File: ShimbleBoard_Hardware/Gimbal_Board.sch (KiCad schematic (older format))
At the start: 85 parts, among them Q1 Q_NMOS_GDS, Q2 Q_NMOS_GDS, Q3 Q_NMOS_GDS, Q4 Q_NMOS_GDS, Q5 Q_NMOS_GDS, Q6 Q_NMOS_GDS, Q7 Q_NMOS_GDS, Q8 Q_NMOS_GDS, SW1 SW_Push, SW10 SW_SPDT, SW2 SW_Push, SW3 SW_Push, SW4 SW_Push, SW5 SW_Push, SW6 SW_Push, SW7 SW_Push, SW8 SW_Push, SW9 SW_Push, U1 TM4C129E_Launchpad, U2 OKI, U3 OKI

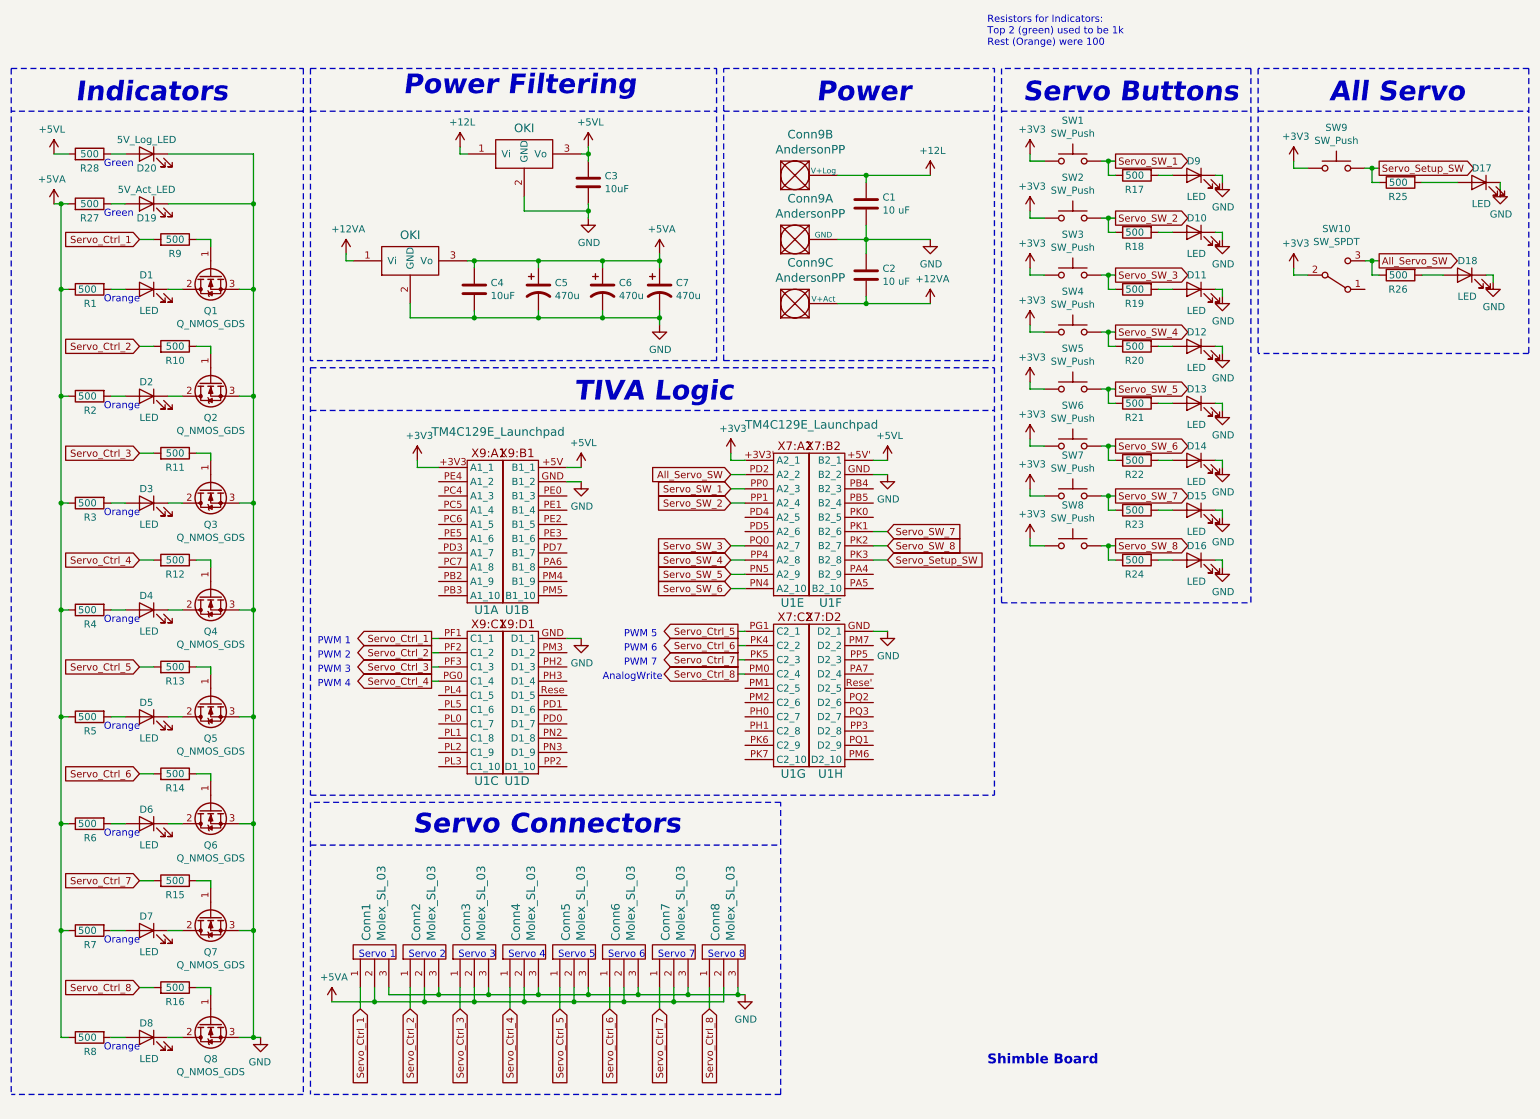
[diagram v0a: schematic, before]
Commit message: Changed the LED's to 5VL and fixed the wiring for it and added X's
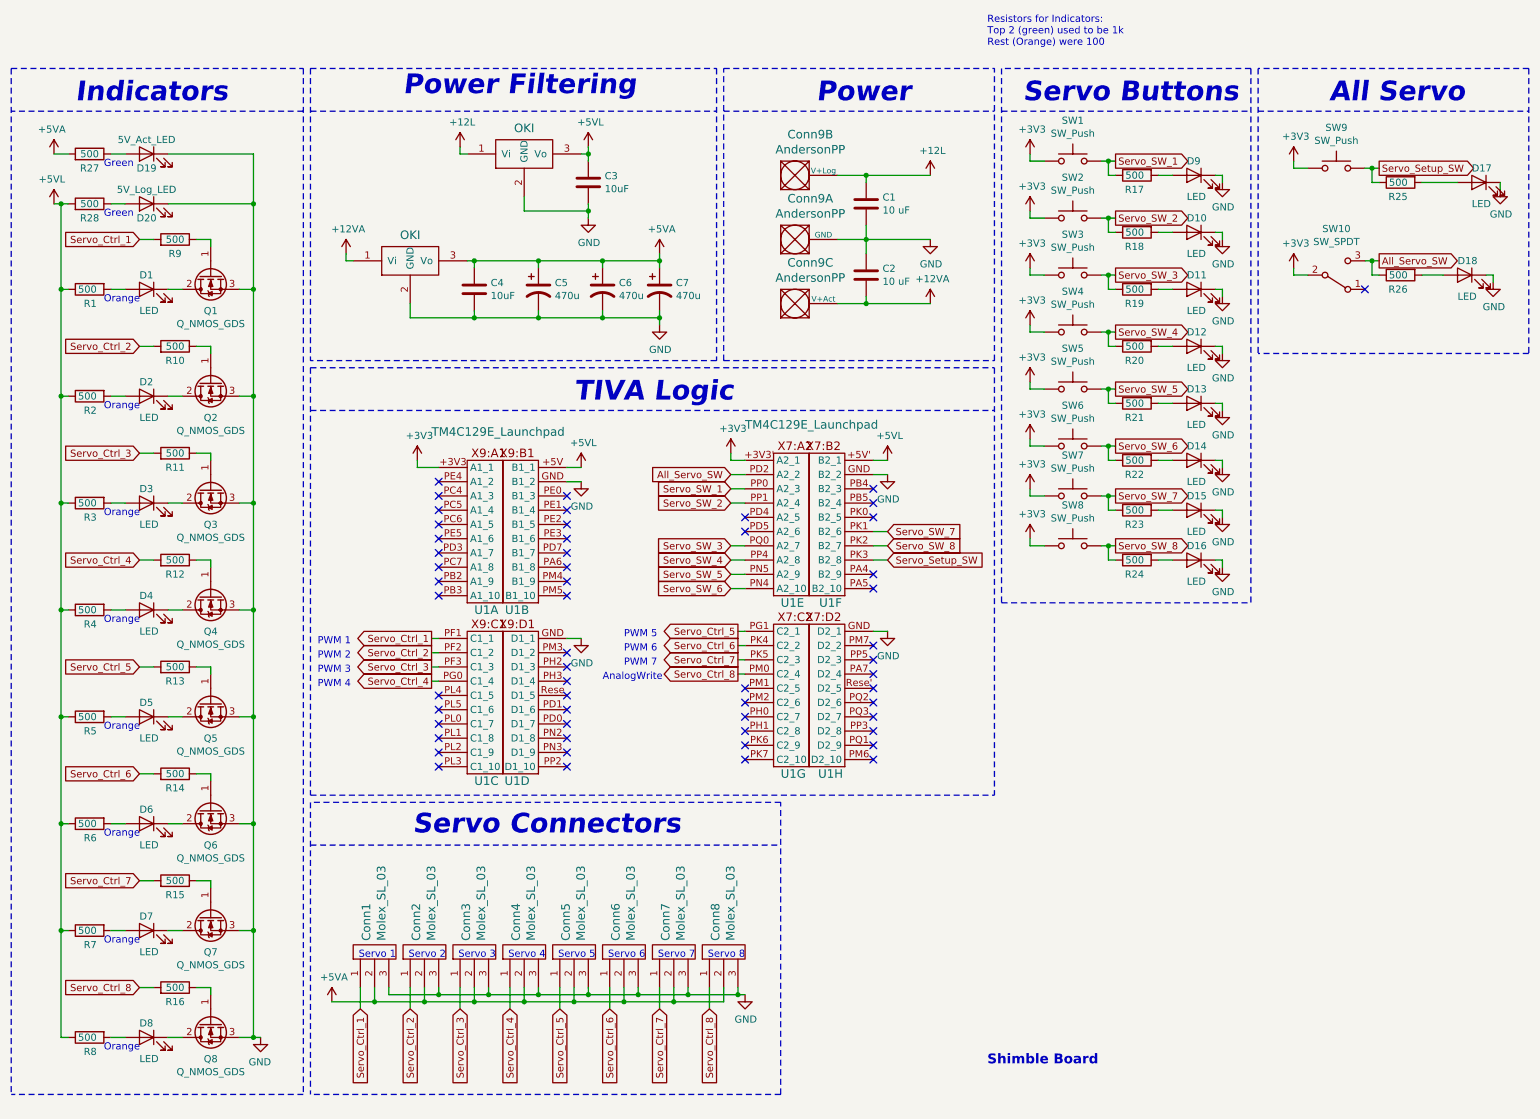
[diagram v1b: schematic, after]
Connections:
- net +5VA: no longer R1.1, R2.1, R3.1, R4.1, R5.1, R6.1, R7.1, R8.1
- net +5VL: now also R1.1, R2.1, R3.1, R4.1, R5.1, R6.1, R7.1, R8.1
- no-connect marks 0 -> 55
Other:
- moved on the sheet: D19, D20, R27, R28
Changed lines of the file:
@@
 L power:+5VA #PWR010
 U 1 1 5D93B52A
-P 800 1450
-F 0 "#PWR010" H 800 1300 50  0001 C CNN
-F 1 "+5VA" H 815 1623 50  0000 C CNN
-F 2 "" H 800 1450 50  0001 C CNN
-F 3 "" H 800 1450 50  0001 C CNN
-	1    800  1450
+P 800 1100
+F 0 "#PWR010" H 800 950 50  0001 C CNN
+F 1 "+5VA" H 815 1273 50  0000 C CNN
+F 2 "" H 800 1100 50  0001 C CNN
+F 3 "" H 800 1100 50  0001 C CNN
+	1    800  1100
 	-1   0    0    -1
 $EndComp
@@
 L Device:LED D19
 U 1 1 5D93B514
-P 1450 1450
-F 0 "D19" H 1450 1350 50  0000 C CNN
-F 1 "5V_Act_LED" H 1450 1550 50  0000 C CNN
-F 2 "Diode_SMD:D_0603_1608Metric_Pad1.05x0.95mm_HandSolder" H 1450 1450 50  0001 C CNN
-F 3 "~" H 1450 1450 50  0001 C CNN
-	1    1450 1450
+P 1450 1100
+F 0 "D19" H 1450 1000 50  0000 C CNN
+F 1 "5V_Act_LED" H 1450 1200 50  0000 C CNN
+F 2 "Diode_SMD:D_0603_1608Metric_Pad1.05x0.95mm_HandSolder" H 1450 1100 50  0001 C CNN
+F 3 "~" H 1450 1100 50  0001 C CNN
+	1    1450 1100
 	-1   0    0    -1
 $EndComp
@@
 L Device:R R27
 U 1 1 5D93B508
-P 1050 1450
-F 0 "R27" V 950 1450 50  0000 C CNN
-F 1 "500" V 1050 1450 50  0000 C CNN
-F 2 "Resistor_SMD:R_0603_1608Metric_Pad1.05x0.95mm_HandSolder" V 980 1450 50  0001 C CNN
-F 3 "~" H 1050 1450 50  0001 C CNN
-	1    1050 1450
+P 1050 1100
+F 0 "R27" V 950 1100 50  0000 C CNN
+F 1 "500" V 1050 1100 50  0000 C CNN
+F 2 "Resistor_SMD:R_0603_1608Metric_Pad1.05x0.95mm_HandSolder" V 980 1100 50  0001 C CNN
+F 3 "~" H 1050 1100 50  0001 C CNN
+	1    1050 1100
 	0    1    -1   0
 $EndComp
@@
 L Device:LED D20
 U 1 1 5D93B50E
-P 1450 1100
-F 0 "D20" H 1450 1000 50  0000 C CNN
-F 1 "5V_Log_LED" H 1450 1200 50  0000 C CNN
-F 2 "Diode_SMD:D_0603_1608Metric_Pad1.05x0.95mm_HandSolder" H 1450 1100 50  0001 C CNN
-F 3 "~" H 1450 1100 50  0001 C CNN
-	1    1450 1100
+P 1450 1450
+F 0 "D20" H 1450 1350 50  0000 C CNN
+F 1 "5V_Log_LED" H 1450 1550 50  0000 C CNN
+F 2 "Diode_SMD:D_0603_1608Metric_Pad1.05x0.95mm_HandSolder" H 1450 1450 50  0001 C CNN
+F 3 "~" H 1450 1450 50  0001 C CNN
+	1    1450 1450
 	-1   0    0    -1
 $EndComp
@@
 L Device:R R28
 U 1 1 5D93B51A
-P 1050 1100
-F 0 "R28" V 950 1100 50  0000 C CNN
-F 1 "500" V 1050 1100 50  0000 C CNN
-F 2 "Resistor_SMD:R_0603_1608Metric_Pad1.05x0.95mm_HandSolder" V 980 1100 50  0001 C CNN
-F 3 "~" H 1050 1100 50  0001 C CNN
-	1    1050 1100
+P 1050 1450
+F 0 "R28" V 950 1450 50  0000 C CNN
+F 1 "500" V 1050 1450 50  0000 C CNN
+F 2 "Resistor_SMD:R_0603_1608Metric_Pad1.05x0.95mm_HandSolder" V 980 1450 50  0001 C CNN
+F 3 "~" H 1050 1450 50  0001 C CNN
+	1    1050 1450
 	0    1    -1   0
 $EndComp
@@
 L power:+5VL #PWR09
 U 1 1 5D93B524
-P 800 1100
-F 0 "#PWR09" H 800 950 50  0001 C CNN
-F 1 "+5VL" H 815 1273 50  0000 C CNN
-F 2 "" H 800 1100 50  0001 C CNN
-F 3 "" H 800 1100 50  0001 C CNN
-	1    800  1100
+P 800 1450
+F 0 "#PWR09" H 800 1300 50  0001 C CNN
+F 1 "+5VL" H 815 1623 50  0000 C CNN
+F 2 "" H 800 1450 50  0001 C CNN
+F 3 "" H 800 1450 50  0001 C CNN
+	1    800  1450
 	-1   0    0    -1
 $EndComp
@@
 Wire Wire Line
 	6950 1250 6500 1250
-$Comp
-L power:+12L #PWR0105
-U 1 1 5DA8971E
-P 6950 1250
-F 0 "#PWR0105" H 6950 1100 50  0001 C CNN
-F 1 "+12L" H 6965 1423 50  0000 C CNN
-F 2 "" H 6950 1250 50  0001 C CNN
-F 3 "" H 6950 1250 50  0001 C CNN
-	1    6950 1250
-	1    0    0    -1
-$EndComp
 $Comp
 L power:+12VA #PWR0104
@@
 Text Notes 9750 750  0    138  Italic 28
 All Servo
+$Comp
+L power:+12L #PWR0105
+U 1 1 5DA8971E
+P 6950 1250
+F 0 "#PWR0105" H 6950 1100 50  0001 C CNN
+F 1 "+12L" H 6965 1423 50  0000 C CNN
+F 2 "" H 6950 1250 50  0001 C CNN
+F 3 "" H 6950 1250 50  0001 C CNN
+	1    6950 1250
+	1    0    0    -1
+$EndComp
+NoConn ~ 4400 3500
+NoConn ~ 4400 3600
+NoConn ~ 4400 3700
+NoConn ~ 4400 3800
+NoConn ~ 4400 3900
+NoConn ~ 4400 4000
+NoConn ~ 4400 4100
+NoConn ~ 4400 4200
+NoConn ~ 3500 4200
+NoConn ~ 3500 4100
+NoConn ~ 3500 4000
+NoConn ~ 3500 3900
+NoConn ~ 3500 3800
+NoConn ~ 3500 3700
+NoConn ~ 3500 3600
+NoConn ~ 3500 3500
+NoConn ~ 3500 3400
+NoConn ~ 3500 4900
+NoConn ~ 3500 5000
+NoConn ~ 3500 5100
+NoConn ~ 3500 5200
+NoConn ~ 3500 5300
+NoConn ~ 3500 5400
+NoConn ~ 4400 5400
+NoConn ~ 4400 5300
+NoConn ~ 4400 5200
+NoConn ~ 4400 5100
+NoConn ~ 4400 5000
+NoConn ~ 4400 4900
+NoConn ~ 4400 4800
+NoConn ~ 4400 4700
+NoConn ~ 4400 4600
+NoConn ~ 5650 4850
+NoConn ~ 5650 4950
+NoConn ~ 5650 5050
+NoConn ~ 5650 5150
+NoConn ~ 5650 5250
+NoConn ~ 5650 5350
+NoConn ~ 6550 5350
+NoConn ~ 6550 5250
+NoConn ~ 6550 5150
+NoConn ~ 6550 5050
+NoConn ~ 6550 4950
+NoConn ~ 6550 4850
+NoConn ~ 6550 4750
+NoConn ~ 6550 4650
+NoConn ~ 6550 4550
+NoConn ~ 6550 4150
+NoConn ~ 6550 4050
+NoConn ~ 5650 3750
+NoConn ~ 5650 3650
+NoConn ~ 6550 3650
+NoConn ~ 6550 3550
+NoConn ~ 6550 3450
+NoConn ~ 10000 2050
 $EndSCHEMATC

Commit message: All but a bit
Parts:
- added D21: 12V_Log_LED, Diode_SMD:D_0603_1608Metric_Pad1.05x0.95mm_HandSolder, symbol Device:LED
- added D22: 12V_Act_LED, Diode_SMD:D_0603_1608Metric_Pad1.05x0.95mm_HandSolder, symbol Device:LED
- added R29, R30: 1000, Resistor_SMD:R_0603_1608Metric_Pad1.05x0.95mm_HandSolder, symbol Device:R
- R17, R18, R19, R20, R21, R22, R23, R24, R25, R26: value 500 -> 330
- U1: footprint MRDT_Shields:TM4C129E_Launchpad_FULL_THT_BOTTOM -> MRDT_Shields:TM4C129E_Launchpad_FULL_THT_BOTTOM_5
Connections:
- net +12L: now also R29.2
- net +12VA: now also R30.2
- net +5VA: now also Conn1.1, Conn2.1, Conn3.1, Conn4.1, Conn5.1, Conn6.1, Conn7.1, Conn8.1; no longer Conn1.2, Conn2.2, Conn3.2, Conn4.2, Conn5.2, Conn6.2, Conn7.2, Conn8.2
- net GND: now also Conn1.2, Conn2.2, Conn3.2, Conn4.2, Conn5.2, Conn6.2, Conn7.2, Conn8.2, D21.1 (K), D22.1 (K); no longer Conn1.3, Conn2.3, Conn3.3, Conn4.3, Conn5.3, Conn6.3, Conn7.3, Conn8.3
- net Servo_Ctrl_1: now also Conn1.3; no longer Conn1.1
- net Servo_Ctrl_2: now also Conn2.3; no longer Conn2.1
- net Servo_Ctrl_3: now also Conn3.3; no longer Conn3.1
- net Servo_Ctrl_4: now also Conn4.3; no longer Conn4.1
- net Servo_Ctrl_5: now also Conn5.3; no longer Conn5.1
- net Servo_Ctrl_6: now also Conn6.3; no longer Conn6.1
- net Servo_Ctrl_7: now also Conn7.3; no longer Conn7.1
- net Servo_Ctrl_8: now also Conn8.3; no longer Conn8.1
- new net: D22.2 (A), R30.1
- new net: D21.2 (A), R29.1
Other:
- note removed: "Resistors for Indicators:\nTop 2 (green) used to be 1k\nRest (Orange) were 100"
- moved on the sheet: D1, D19, D2, D20, D3, D4, D5, D6, D7, Q1, Q2, Q3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

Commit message: Added signatures
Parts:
- U1: footprint MRDT_Shields:TM4C129E_Launchpad_FULL_THT_BOTTOM_5 -> ShimbleBoard_Hardware:TM4C129E_Launchpad_FULL_THT_BOTTOM_5
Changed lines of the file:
@@
 F 0 "U1" H 5900 4150 60  0000 L CNN
 F 1 "TM4C129E_Launchpad" H 5650 5400 60  0000 L CNN
-F 2 "MRDT_Shields:TM4C129E_Launchpad_FULL_THT_BOTTOM_5" H 5850 4200 60  0001 C CNN
+F 2 "ShimbleBoard_Hardware:TM4C129E_Launchpad_FULL_THT_BOTTOM_5" H 5850 4200 60  0001 C CNN
 F 3 "" H 5850 4200 60  0001 C CNN
 	5    5850 4200
@@
 F 0 "U1" H 6450 5350 60  0000 C CNN
 F 1 "TM4C129E_Launchpad" H 5550 5400 60  0001 C CNN
-F 2 "MRDT_Shields:TM4C129E_Launchpad_FULL_THT_BOTTOM_5" H 6350 5400 60  0001 C CNN
+F 2 "ShimbleBoard_Hardware:TM4C129E_Launchpad_FULL_THT_BOTTOM_5" H 6350 5400 60  0001 C CNN
 F 3 "" H 6350 5400 60  0001 C CNN
 	8    6350 5400
@@
 F 0 "U1" H 5900 5350 60  0000 L CNN
 F 1 "TM4C129E_Launchpad" H 4550 5400 60  0001 L CNN
-F 2 "MRDT_Shields:TM4C129E_Launchpad_FULL_THT_BOTTOM_5" H 5850 5400 60  0001 C CNN
+F 2 "ShimbleBoard_Hardware:TM4C129E_Launchpad_FULL_THT_BOTTOM_5" H 5850 5400 60  0001 C CNN
 F 3 "" H 5850 5400 60  0001 C CNN
 	7    5850 5400
@@
 F 0 "U1" H 6450 4150 60  0000 C CNN
 F 1 "TM4C129E_Launchpad" H 5600 4200 60  0001 C CNN
-F 2 "MRDT_Shields:TM4C129E_Launchpad_FULL_THT_BOTTOM_5" H 6350 4200 60  0001 C CNN
+F 2 "ShimbleBoard_Hardware:TM4C129E_Launchpad_FULL_THT_BOTTOM_5" H 6350 4200 60  0001 C CNN
 F 3 "" H 6350 4200 60  0001 C CNN
 	6    6350 4200
@@
 F 0 "U1" H 4350 5400 60  0000 C CNN
 F 1 "TM4C129E_Launchpad" H 4505 5942 60  0001 L CNN
-F 2 "MRDT_Shields:TM4C129E_Launchpad_FULL_THT_BOTTOM_5" H 4200 5450 60  0001 C CNN
+F 2 "ShimbleBoard_Hardware:TM4C129E_Launchpad_FULL_THT_BOTTOM_5" H 4200 5450 60  0001 C CNN
 F 3 "" H 4200 5450 60  0001 C CNN
 	4    4200 5450
@@
 F 0 "U1" H 3750 5400 60  0000 L CNN
 F 1 "TM4C129E_Launchpad" H 4005 5942 60  0001 L CNN
-F 2 "MRDT_Shields:TM4C129E_Launchpad_FULL_THT_BOTTOM_5" H 3700 5450 60  0001 C CNN
+F 2 "ShimbleBoard_Hardware:TM4C129E_Launchpad_FULL_THT_BOTTOM_5" H 3700 5450 60  0001 C CNN
 F 3 "" H 3700 5450 60  0001 C CNN
 	3    3700 5450
@@
 F 0 "U1" H 4350 4200 60  0000 C CNN
 F 1 "TM4C129E_Launchpad" H 4231 5421 60  0001 C CNN
-F 2 "MRDT_Shields:TM4C129E_Launchpad_FULL_THT_BOTTOM_5" H 4200 4250 60  0001 C CNN
+F 2 "ShimbleBoard_Hardware:TM4C129E_Launchpad_FULL_THT_BOTTOM_5" H 4200 4250 60  0001 C CNN
 F 3 "" H 4200 4250 60  0001 C CNN
 	2    4200 4250
@@
 F 0 "U1" H 3750 4200 60  0000 L CNN
 F 1 "TM4C129E_Launchpad" H 3450 5450 60  0000 L CNN
-F 2 "MRDT_Shields:TM4C129E_Launchpad_FULL_THT_BOTTOM_5" H 3700 4250 60  0001 C CNN
+F 2 "ShimbleBoard_Hardware:TM4C129E_Launchpad_FULL_THT_BOTTOM_5" H 3700 4250 60  0001 C CNN
 F 3 "" H 3700 4250 60  0001 C CNN
 	1    3700 4250

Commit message: Trying to figure out how to make a bom
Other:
- moved on the sheet: D17

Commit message: Different shield
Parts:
- U1: footprint ShimbleBoard_Hardware:TM4C129E_Launchpad_FULL_THT_BOTTOM_5 -> MRDT_Shields:TM4C129E_Launchpad_FULL_THT_BOTTOM
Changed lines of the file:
@@
 F 0 "U1" H 5900 4150 60  0000 L CNN
 F 1 "TM4C129E_Launchpad" H 5650 5400 60  0000 L CNN
-F 2 "ShimbleBoard_Hardware:TM4C129E_Launchpad_FULL_THT_BOTTOM_5" H 5850 4200 60  0001 C CNN
+F 2 "MRDT_Shields:TM4C129E_Launchpad_FULL_THT_BOTTOM" H 5850 4200 60  0001 C CNN
 F 3 "" H 5850 4200 60  0001 C CNN
 	5    5850 4200
@@
 F 0 "U1" H 6450 5350 60  0000 C CNN
 F 1 "TM4C129E_Launchpad" H 5550 5400 60  0001 C CNN
-F 2 "ShimbleBoard_Hardware:TM4C129E_Launchpad_FULL_THT_BOTTOM_5" H 6350 5400 60  0001 C CNN
+F 2 "MRDT_Shields:TM4C129E_Launchpad_FULL_THT_BOTTOM" H 6350 5400 60  0001 C CNN
 F 3 "" H 6350 5400 60  0001 C CNN
 	8    6350 5400
@@
 F 0 "U1" H 5900 5350 60  0000 L CNN
 F 1 "TM4C129E_Launchpad" H 4550 5400 60  0001 L CNN
-F 2 "ShimbleBoard_Hardware:TM4C129E_Launchpad_FULL_THT_BOTTOM_5" H 5850 5400 60  0001 C CNN
+F 2 "MRDT_Shields:TM4C129E_Launchpad_FULL_THT_BOTTOM" H 5850 5400 60  0001 C CNN
 F 3 "" H 5850 5400 60  0001 C CNN
 	7    5850 5400
@@
 F 0 "U1" H 6450 4150 60  0000 C CNN
 F 1 "TM4C129E_Launchpad" H 5600 4200 60  0001 C CNN
-F 2 "ShimbleBoard_Hardware:TM4C129E_Launchpad_FULL_THT_BOTTOM_5" H 6350 4200 60  0001 C CNN
+F 2 "MRDT_Shields:TM4C129E_Launchpad_FULL_THT_BOTTOM" H 6350 4200 60  0001 C CNN
 F 3 "" H 6350 4200 60  0001 C CNN
 	6    6350 4200
@@
 F 0 "U1" H 4350 5400 60  0000 C CNN
 F 1 "TM4C129E_Launchpad" H 4505 5942 60  0001 L CNN
-F 2 "ShimbleBoard_Hardware:TM4C129E_Launchpad_FULL_THT_BOTTOM_5" H 4200 5450 60  0001 C CNN
+F 2 "MRDT_Shields:TM4C129E_Launchpad_FULL_THT_BOTTOM" H 4200 5450 60  0001 C CNN
 F 3 "" H 4200 5450 60  0001 C CNN
 	4    4200 5450
@@
 F 0 "U1" H 3750 5400 60  0000 L CNN
 F 1 "TM4C129E_Launchpad" H 4005 5942 60  0001 L CNN
-F 2 "ShimbleBoard_Hardware:TM4C129E_Launchpad_FULL_THT_BOTTOM_5" H 3700 5450 60  0001 C CNN
+F 2 "MRDT_Shields:TM4C129E_Launchpad_FULL_THT_BOTTOM" H 3700 5450 60  0001 C CNN
 F 3 "" H 3700 5450 60  0001 C CNN
 	3    3700 5450
@@
 F 0 "U1" H 4350 4200 60  0000 C CNN
 F 1 "TM4C129E_Launchpad" H 4231 5421 60  0001 C CNN
-F 2 "ShimbleBoard_Hardware:TM4C129E_Launchpad_FULL_THT_BOTTOM_5" H 4200 4250 60  0001 C CNN
+F 2 "MRDT_Shields:TM4C129E_Launchpad_FULL_THT_BOTTOM" H 4200 4250 60  0001 C CNN
 F 3 "" H 4200 4250 60  0001 C CNN
 	2    4200 4250
@@
 F 0 "U1" H 3750 4200 60  0000 L CNN
 F 1 "TM4C129E_Launchpad" H 3450 5450 60  0000 L CNN
-F 2 "ShimbleBoard_Hardware:TM4C129E_Launchpad_FULL_THT_BOTTOM_5" H 3700 4250 60  0001 C CNN
+F 2 "MRDT_Shields:TM4C129E_Launchpad_FULL_THT_BOTTOM" H 3700 4250 60  0001 C CNN
 F 3 "" H 3700 4250 60  0001 C CNN
 	1    3700 4250

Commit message: Minor changes
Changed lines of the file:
@@
 L power:GND #PWR011
 U 1 1 5D99FADA
-P 2250 7300
-F 0 "#PWR011" H 2250 7050 50  0001 C CNN
-F 1 "GND" H 2255 7127 50  0000 C CNN
-F 2 "" H 2250 7300 50  0001 C CNN
-F 3 "" H 2250 7300 50  0001 C CNN
-	1    2250 7300
+P 2200 7350
+F 0 "#PWR011" H 2200 7100 50  0001 C CNN
+F 1 "GND" H 2200 7200 50  0000 C CNN
+F 2 "" H 2200 7350 50  0001 C CNN
+F 3 "" H 2200 7350 50  0001 C CNN
+	1    2200 7350
 	-1   0    0    -1
 $EndComp
@@
 Servo_Ctrl_7
 Wire Wire Line
-	2200 7300 2250 7300
+	2200 7300 2200 7350
 $Comp
 L Device:Q_NMOS_GDS Q3
@@
 F 3 "" H 2850 1800 50  0001 C CNN
 	1    2850 1800
-	1    0    0    -1
-$EndComp
-$Comp
-L MRDT_Devices:OKI U3
-U 1 1 5DAB88C5
-P 3100 1950
-F 0 "U3" H 3150 1900 60  0001 C CNN
-F 1 "OKI" H 3300 2231 60  0000 C CNN
-F 2 "MRDT_Devices:OKI_Horizontal" H 2900 1850 60  0001 C CNN
-F 3 "" H 2900 1850 60  0001 C CNN
-	1    3100 1950
 	1    0    0    -1
 $EndComp
@@
 P 2800 7000
 F 0 "#PWR01" H 2800 6850 50  0001 C CNN
-F 1 "+5VA" H 2815 7173 50  0000 C CNN
+F 1 "+5VA" H 2750 7150 50  0000 C CNN
 F 2 "" H 2800 7000 50  0001 C CNN
 F 3 "" H 2800 7000 50  0001 C CNN
@@
 U 1 1 5DC3CA06
 P 10700 1300
-F 0 "D17" H 10750 1400 50  0000 R CNN
+F 0 "D17" H 10650 1400 50  0000 R CNN
 F 1 "LED" H 10750 1150 50  0000 R CNN
 F 2 "Diode_SMD:D_0603_1608Metric_Pad1.05x0.95mm_HandSolder" H 10700 1300 50  0001 C CNN
@@
 	10900 1300 10900 1950
 Connection ~ 10900 1950
+$Comp
+L MRDT_Devices:OKI U3
+U 1 1 5DAB88C5
+P 3100 1950
+F 0 "U3" H 3150 1900 60  0001 C CNN
+F 1 "OKI" H 3300 2231 60  0000 C CNN
+F 2 "MRDT_Devices:OKI_Horizontal" H 2900 1850 60  0001 C CNN
+F 3 "" H 2900 1850 60  0001 C CNN
+	1    3100 1950
+	1    0    0    -1
+$EndComp
 $EndSCHEMATC
